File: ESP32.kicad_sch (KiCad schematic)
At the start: 1 part, among them U1 ESP32-C3-WROOM-02

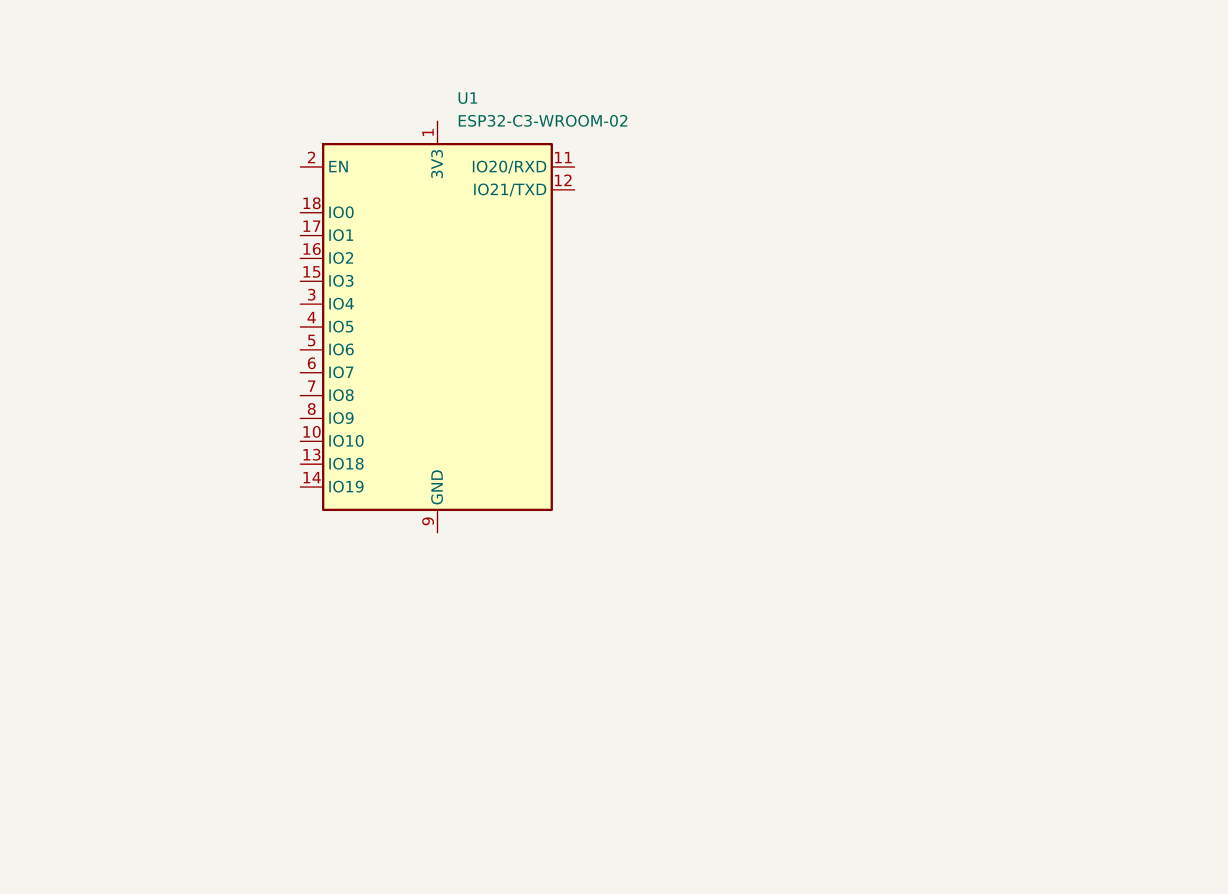
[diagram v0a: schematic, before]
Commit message: Concluded ESP32 + Power
still need to have a look around for errors
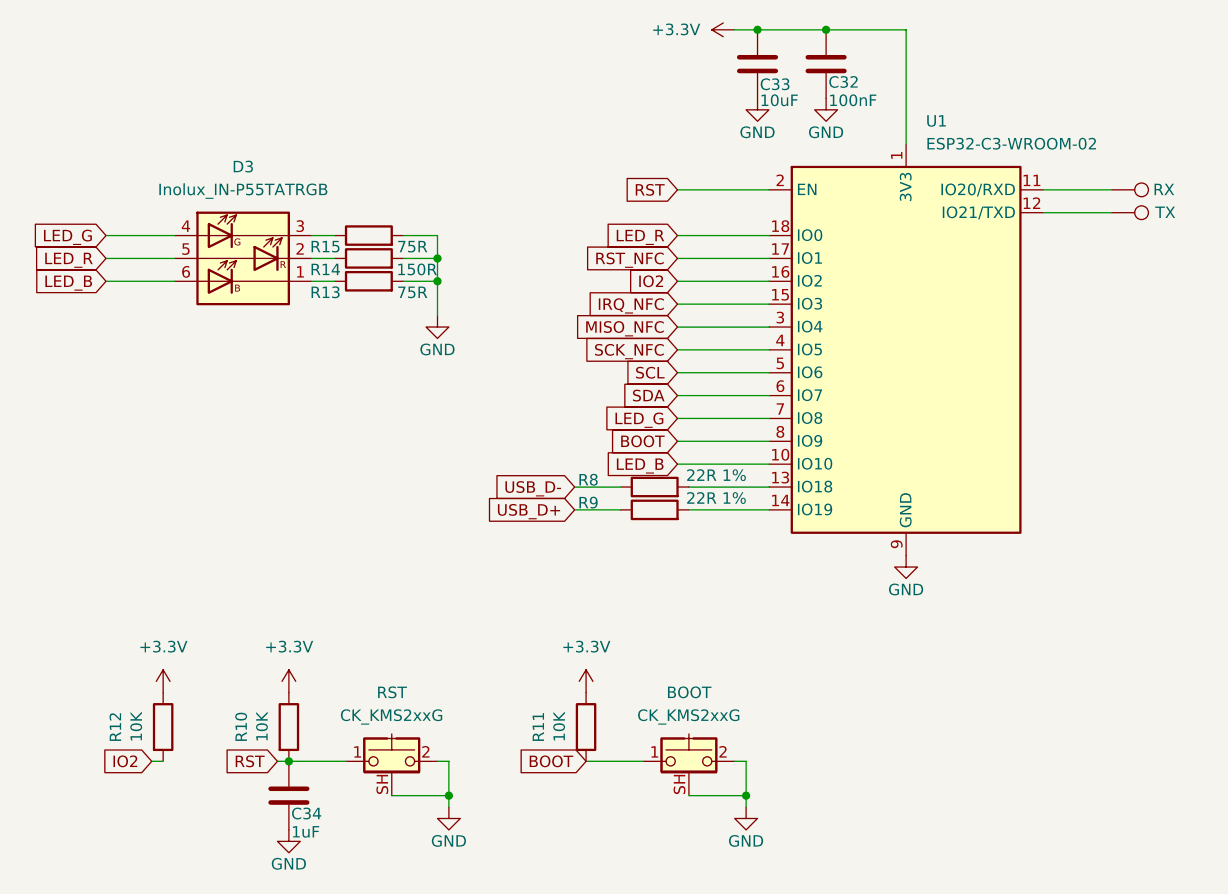
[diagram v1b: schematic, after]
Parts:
- added BOOT, RST: CK_KMS2xxG, Button_Switch_SMD:SW_SPST_CK_KMS2xxGP, symbol Switch:CK_KMS2xxG
- added C32: 100nF, Capacitor_SMD:C_0603_1608Metric, symbol Device:C
- added C33: 10uF, Capacitor_SMD:C_0805_2012Metric, symbol Device:C
- added C34: 1uF, Capacitor_SMD:C_0603_1608Metric, symbol Device:C
- added D3: Inolux_IN-P55TATRGB, LED_SMD:LED_Inolux_IN-P55TATRGB_PLCC6_5.0x5.5mm_P1.8mm, symbol LED:Inolux_IN-P55TATRGB
- added R10, R11, R12: 10K, RevK:R_0603, symbol Device:R
- added R13, R15: 75R, RevK:R_0603, symbol Device:R
- added R14: 150R, RevK:R_0603, symbol Device:R
- added R8, R9: 22R 1%, RevK:R_0603, symbol Device:R
- added RX, TX: TestPoint, TestPoint:TestPoint_THTPad_1.5x1.5mm_Drill0.7mm, symbol Connector:TestPoint
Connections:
- net +3.3V: now reaches U1.1 (3V3)
- net +3.3V: now also C32.2, C33.1, R10.1, R11.1, R12.1
- net LED_B: now reaches U1.10 (IO10)
- net LED_B: now also D3.6 (AB)
- net at U1.11 (IO20/RXD): now also RX.1
- net at U1.12 (IO21/TXD): now also TX.1
- net at U1.13 (IO18): now also R8.2
- net at U1.14 (IO19): now also R9.2
- net IRQ_NFC: now reaches U1.15 (IO3)
- net IO2: now reaches U1.16 (IO2)
- net IO2: now also R12.2
- net RST_NFC: now reaches U1.17 (IO1)
- net LED_R: now reaches U1.18 (IO0)
- net LED_R: now also D3.5 (AR)
- net GND: now reaches U1.19 (GND), U1.9 (GND)
- net GND: now also BOOT.2, BOOT.SH (B), C32.1, C33.2, C34.1, R13.2, R14.2, R15.2, RST.2, RST.SH (B)
- net RST: now reaches U1.2 (EN)
- net RST: now also C34.2, R10.2, RST.1
- net MISO_NFC: now reaches U1.3 (IO4)
- net SCK_NFC: now reaches U1.4 (IO5)
- net SCL: now reaches U1.5 (IO6)
- net SDA: now reaches U1.6 (IO7)
- net LED_G: now reaches U1.7 (IO8)
- net LED_G: now also D3.4 (AG)
- net BOOT: now reaches U1.8 (IO9)
- net BOOT: now also BOOT.1, R11.2
- new net: D3.3 (KG), R15.1
- new net: D3.1 (KB), R13.1
- new net: D3.2 (KR), R14.1
- new net USB_D+: R9.1
- new net USB_D-: R8.1
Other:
- moved on the sheet: U1

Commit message: Added Revs + PDF
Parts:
- renumbered BOOT to BOOT1, RST to RST1, RX to RX1, TX to TX1
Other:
- title: (none) -> Homekey PCB ESP32C3
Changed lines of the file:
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@@
 	(generator_version "8.0")
 	(paper "A4")
+	(title_block
+		(title "Homekey PCB ESP32C3")
+		(date "2024-07-03")
+		(rev "Rev A")
+	)
 	(junction
 		(at 100.33 149.86)
@@
 		(on_board yes)
 		(dnp no)
-		(property "Reference" "TX"
+		(property "Reference" "TX1"
 			(at 178.816 85.09 90)
 			(effects
@@
 			(project ""
 				(path "/8ef12b84-4556-413e-8e5a-ce52402aeac0/41d98d3b-40e8-42b4-9eac-bd82a45a039c"
-					(reference "TX")
+					(reference "TX1")
 					(unit 1)
 				)
@@
 		(on_board yes)
 		(dnp no)
-		(property "Reference" "RX"
+		(property "Reference" "RX1"
 			(at 178.562 82.55 90)
 			(effects
@@
 			(project "Homekey"
 				(path "/8ef12b84-4556-413e-8e5a-ce52402aeac0/41d98d3b-40e8-42b4-9eac-bd82a45a039c"
-					(reference "RX")
+					(reference "RX1")
 					(unit 1)
 				)
@@
 		(dnp no)
 		(fields_autoplaced yes)
-		(property "Reference" "BOOT"
+		(property "Reference" "BOOT1"
 			(at 127 138.43 0)
 			(effects
@@
 			(project "Homekey"
 				(path "/8ef12b84-4556-413e-8e5a-ce52402aeac0/41d98d3b-40e8-42b4-9eac-bd82a45a039c"
-					(reference "BOOT")
+					(reference "BOOT1")
 					(unit 1)
 				)
@@
 		(dnp no)
 		(fields_autoplaced yes)
-		(property "Reference" "RST"
+		(property "Reference" "RST1"
 			(at 93.98 138.43 0)
 			(effects
@@
 			(project "Homekey"
 				(path "/8ef12b84-4556-413e-8e5a-ce52402aeac0/41d98d3b-40e8-42b4-9eac-bd82a45a039c"
-					(reference "RST")
+					(reference "RST1")
 					(unit 1)
 				)

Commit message: Start of layout
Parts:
- R10, R11, R12, R13, R14, R15, R8, R9: footprint RevK:R_0603 -> Resistor_SMD_AKL:R_0603_1608Metric; symbol Device:R -> PCM_Resistor_AKL:R_0603
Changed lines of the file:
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@@
 	)
 	(symbol
-		(lib_id "Device:R")
+		(lib_id "PCM_Resistor_AKL:R_0603")
 		(at 82.55 142.24 0)
 		(unit 1)
@@
 			)
 		)
-		(property "Footprint" "RevK:R_0603"
-			(at 80.772 142.24 90)
+		(property "Footprint" "Resistor_SMD_AKL:R_0603_1608Metric"
+			(at 82.55 153.67 0)
 			(effects
 				(font
@@
 	)
 	(symbol
-		(lib_id "Device:R")
+		(lib_id "PCM_Resistor_AKL:R_0603")
 		(at 115.57 142.24 0)
 		(unit 1)
@@
 			)
 		)
-		(property "Footprint" "RevK:R_0603"
-			(at 113.792 142.24 90)
+		(property "Footprint" "Resistor_SMD_AKL:R_0603_1608Metric"
+			(at 115.57 153.67 0)
 			(effects
 				(font
@@
 	)
 	(symbol
-		(lib_id "Device:R")
+		(lib_id "PCM_Resistor_AKL:R_0603")
 		(at 123.19 115.57 90)
 		(unit 1)
@@
 			)
 		)
-		(property "Footprint" "RevK:R_0603"
-			(at 123.19 117.348 90)
+		(property "Footprint" "Resistor_SMD_AKL:R_0603_1608Metric"
+			(at 134.62 115.57 0)
 			(effects
 				(font
@@
 	)
 	(symbol
-		(lib_id "Device:R")
+		(lib_id "PCM_Resistor_AKL:R_0603")
 		(at 91.44 87.63 90)
 		(unit 1)
@@
 			)
 		)
-		(property "Footprint" "RevK:R_0603"
-			(at 91.44 89.408 90)
+		(property "Footprint" "Resistor_SMD_AKL:R_0603_1608Metric"
+			(at 102.87 87.63 0)
 			(effects
 				(font
@@
 	)
 	(symbol
-		(lib_id "Device:R")
+		(lib_id "PCM_Resistor_AKL:R_0603")
 		(at 68.58 142.24 0)
 		(unit 1)
@@
 			)
 		)
-		(property "Footprint" "RevK:R_0603"
-			(at 66.802 142.24 90)
+		(property "Footprint" "Resistor_SMD_AKL:R_0603_1608Metric"
+			(at 68.58 153.67 0)
 			(effects
 				(font
@@
 	)
 	(symbol
-		(lib_id "Device:R")
+		(lib_id "PCM_Resistor_AKL:R_0603")
 		(at 123.19 118.11 90)
 		(unit 1)
@@
 			)
 		)
-		(property "Footprint" "RevK:R_0603"
-			(at 123.19 119.888 90)
+		(property "Footprint" "Resistor_SMD_AKL:R_0603_1608Metric"
+			(at 134.62 118.11 0)
 			(effects
 				(font
@@
 	)
 	(symbol
-		(lib_id "Device:R")
+		(lib_id "PCM_Resistor_AKL:R_0603")
 		(at 91.44 92.71 90)
 		(unit 1)
@@
 			)
 		)
-		(property "Footprint" "RevK:R_0603"
-			(at 91.44 94.488 90)
+		(property "Footprint" "Resistor_SMD_AKL:R_0603_1608Metric"
+			(at 102.87 92.71 0)
 			(effects
 				(font
@@
 	)
 	(symbol
-		(lib_id "Device:R")
+		(lib_id "PCM_Resistor_AKL:R_0603")
 		(at 91.44 90.17 90)
 		(unit 1)
@@
 			)
 		)
-		(property "Footprint" "RevK:R_0603"
-			(at 91.44 91.948 90)
-			(effects
-				(font
+		(property "Footprint" "Resistor_SMD_AKL:R_0603_1608Metric"
+			(at 102.87 90.17 0)
+			(effects
+				(font

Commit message: Finished rev A PCB V 0.1
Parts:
- added GND1: TestPoint, TestPoint:TestPoint_THTPad_1.5x1.5mm_Drill0.7mm, symbol Connector:TestPoint
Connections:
- net GND: now also GND1.1
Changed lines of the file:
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@@
+	)
+	(symbol
+		(lib_id "Connector:TestPoint")
+		(at 173.99 88.9 270)
+		(unit 1)
+		(exclude_from_sim no)
+		(in_bom yes)
+		(on_board yes)
+		(dnp no)
+		(property "Reference" "GND1"
+			(at 178.816 88.9 90)
+			(effects
+				(font
+					(size 1.27 1.27)
+				)
+				(justify left)
+			)
+		)
+		(property "Value" "TestPoint"
+			(at 179.07 90.1699 90)
+			(effects
+				(font
+					(size 1.27 1.27)
+				)
+				(justify left)
+				(hide yes)
+			)
+		)
+		(property "Footprint" "TestPoint:TestPoint_THTPad_1.5x1.5mm_Drill0.7mm"
+			(at 173.99 93.98 0)
+			(effects
+				(font
+					(size 1.27 1.27)
+				)
+				(hide yes)
+			)
+		)
+		(property "Datasheet" "~"
+			(at 173.99 93.98 0)
+			(effects
+				(font
+					(size 1.27 1.27)
+				)
+				(hide yes)
+			)
+		)
+		(property "Description" "test point"
+			(at 173.99 88.9 0)
+			(effects
+				(font
+					(size 1.27 1.27)
+				)
+				(hide yes)
+			)
+		)
+		(pin "1"
+		)
+		(instances
+			(project "Homekey"
+				(path "/8ef12b84-4556-413e-8e5a-ce52402aeac0/41d98d3b-40e8-42b4-9eac-bd82a45a039c"
+					(reference "GND1")
+					(unit 1)
+				)
+			)
+		)
 	)
 	(symbol
@@
 					(unit 1)
 				)
+			)
+		)
+	)
+	(symbol
+		(lib_id "power:GND")
+		(at 173.99 88.9 0)
+		(unit 1)
+		(exclude_from_sim no)
+		(in_bom yes)
+		(on_board yes)
+		(dnp no)
+		(property "Reference" "#PWR052"
+			(at 173.99 95.25 0)
+			(effects
+				(font
+					(size 1.27 1.27)
+				)
+				(hide yes)
+			)
+		)
+		(property "Value" "GND"
+			(at 173.99 92.71 0)
+			(effects
+				(font
+					(size 1.27 1.27)
+				)
+			)
+		)
+		(property "Footprint" ""
+			(at 173.99 88.9 0)
+			(effects
+				(font
+					(size 1.27 1.27)
+				)
+				(hide yes)
+			)
+		)
+		(property "Datasheet" ""
+			(at 173.99 88.9 0)
+			(effects
+				(font
+					(size 1.27 1.27)
+				)
+				(hide yes)
+			)
+		)
+		(property "Description" "Power symbol creates a global label with name \"GND\" , ground"
+			(at 173.99 88.9 0)
+			(effects
+				(font
+					(size 1.27 1.27)
+				)
+				(hide yes)
+			)
+		)
+		(pin "1"
+		)
+		(instances
+			(project "Homekey"
+				(path "/8ef12b84-4556-413e-8e5a-ce52402aeac0/41d98d3b-40e8-42b4-9eac-bd82a45a039c"
+					(reference "#PWR052")
+					(unit 1)
+				)
